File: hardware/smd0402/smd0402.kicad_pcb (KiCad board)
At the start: 2 copper layers, 150 x 146.5 mm, 140 parts, among them J1 Conn_01x03, J2 SAO v1.69bis addon, J3 SAO v1.69bis badge, P1 Conn_01x02, P2 Conn_01x02, P3 Conn_01x02, P4 Conn_01x02, P5 Conn_01x02, P6 Conn_01x02, U1 WCH CH32V003F4U6

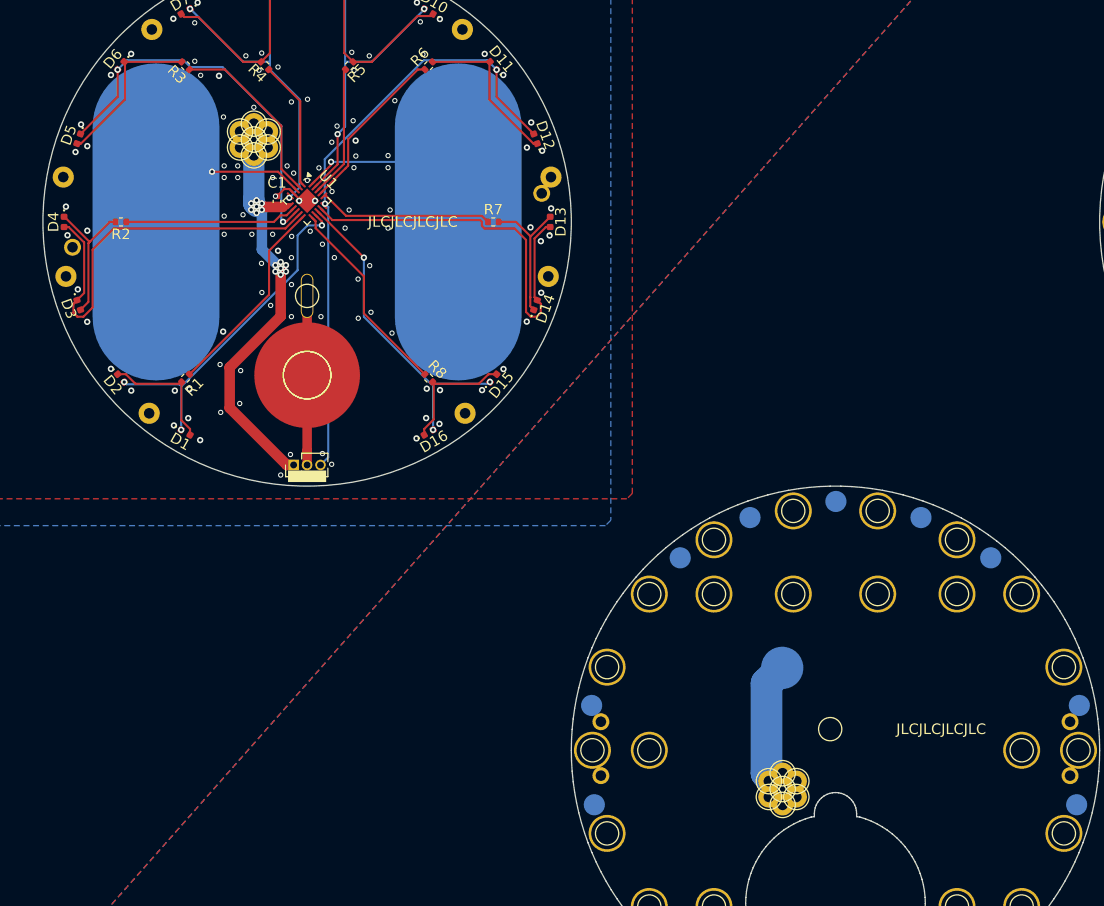
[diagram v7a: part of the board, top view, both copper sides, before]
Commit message: shrink touchpad to 8mm circle
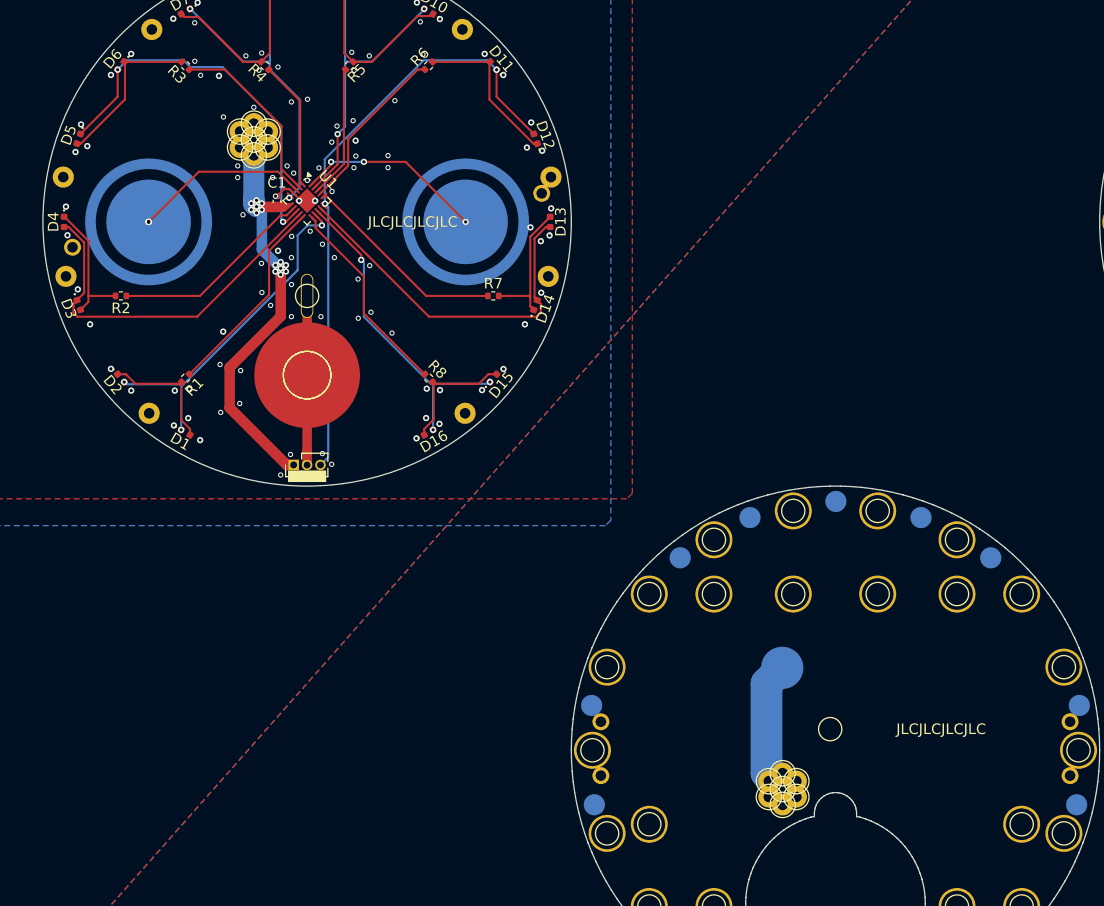
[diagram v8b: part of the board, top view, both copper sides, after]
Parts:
- moved R2 7.00 mm to (32.4, 57.0)
- moved R7 7.00 mm to (67.6, 57.0)
- moved clearance-R2 7.00 mm to (82.4, 107.0)
- moved clearance-R7 7.00 mm to (117.6, 107.0)
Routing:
- net /touch2: track 8.69 -> 16.7 mm, vias 1 -> 3
- net GP7: track 38.6 -> 34.4 mm
- net GP2: track 38.3 -> 35.1 mm
- net PWM2: track 16.3 -> 19.2 mm
- net PWM7: track 16.5 -> 19.4 mm
- net Net-(D3-A): track 13.5 -> 12.7 mm
- net /touch1: track 17.2 -> 17.9 mm, vias 1 -> 3
- net Net-(D13-A): track 13.3 -> 12.7 mm
- net GND: vias 129 -> 118
